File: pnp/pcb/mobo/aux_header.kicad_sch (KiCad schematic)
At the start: 1 part, among them J18 AUX

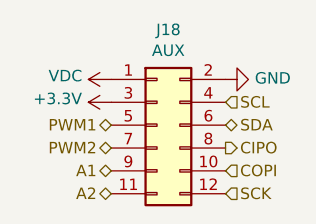
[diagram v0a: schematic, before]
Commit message: first commit of rev04 mobo beta 0. makes solder-selectable jumpers on back side of board not jumped to work with kit drivers, y2 motor port rotated correctly, moves traces out from underneath solder jumpers, adds 0 ohm jumpers to bypass the usb hub, adds 4 pin DIN connector for power, adds large decoupling cap on power supply input to decrease rippling, changes diode choice for 5v multiplexer to one already in the BOM, flips resistors on mos1 to be less confusing
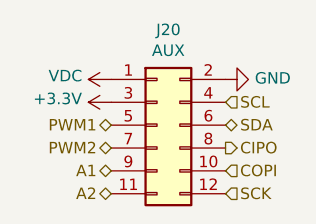
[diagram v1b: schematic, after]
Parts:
- renumbered J18 to J20
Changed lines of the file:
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@@
     (effects (font (size 1.27 1.27)) (justify left))
   )
-  (symbol (lib_id "power:GND") (at 151.13 92.075 90) (unit 1)
+  (symbol (lib_id "power:GND") (at 151.13 92.075 90)
     (in_bom yes) (on_board yes)
-    (property "Reference" "#PWR0232" (id 0) (at 157.48 92.075 0)
+    (property "Reference" "#PWR0235" (id 0) (at 157.48 92.075 0)
       (effects (font (size 1.27 1.27)) hide)
     )
@@
     (pin "1")
   )
-  (symbol (lib_id "power:VDC") (at 138.43 92.075 90) (unit 1)
+  (symbol (lib_id "power:VDC") (at 138.43 92.075 90)
     (in_bom yes) (on_board yes)
-    (property "Reference" "#PWR0230" (id 0) (at 140.97 92.075 0)
+    (property "Reference" "#PWR0233" (id 0) (at 140.97 92.075 0)
       (effects (font (size 1.27 1.27)) hide)
     )
@@
     (pin "1")
   )
-  (symbol (lib_id "Connector_Generic:Conn_02x06_Odd_Even") (at 143.51 97.155 0) (unit 1)
+  (symbol (lib_id "Connector_Generic:Conn_02x06_Odd_Even") (at 143.51 97.155 0)
     (in_bom yes) (on_board yes)
-    (property "Reference" "J18" (id 0) (at 144.78 86.5632 0))
+    (property "Reference" "J20" (id 0) (at 144.78 86.5632 0))
     (property "Value" "AUX" (id 1) (at 144.78 88.8746 0))
     (property "Footprint" "Connector_IDC:IDC-Header_2x06_P2.54mm_Vertical" (id 2) (at 143.51 97.155 0)
@@
     (pin "9")
   )
-  (symbol (lib_id "power:+3.3V") (at 138.43 94.615 90) (unit 1)
+  (symbol (lib_id "power:+3.3V") (at 138.43 94.615 90)
     (in_bom yes) (on_board yes)
-    (property "Reference" "#PWR0231" (id 0) (at 142.24 94.615 0)
+    (property "Reference" "#PWR0234" (id 0) (at 142.24 94.615 0)
       (effects (font (size 1.27 1.27)) hide)
     )
